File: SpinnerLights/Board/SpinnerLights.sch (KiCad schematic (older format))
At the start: 4 parts

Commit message: WIP on SpinnerLights board
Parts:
- removed C?: CP, symbol Device:CP
- removed R?: R, symbol Device:R
- added BT1: Battery_Cell, symbol Device:Battery_Cell
- added C1: 0.1uF, symbol Device:C
- added D1: D, symbol Device:D
- added JP1, JP?: Jumper_2_Open, symbol Jumper:Jumper_2_Open
- added PIXEL2, PIXEL3, PIXEL4, PIXEL5, PIXEL6, Pixel1: NeoPixel_THT, symbol LED:NeoPixel_THT
- added R1: 10K, symbol Device:R
- added R2: 5K, symbol Device:R
- added R3: 400, symbol Device:R
- added U2: ADXL343, Package_LGA:LGA-14_3x5mm_P0.8mm_LayoutBorder1x6y, symbol Sensor_Motion:ADXL343
- gave numbers to parts that had none: 2
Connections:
- net at BT2.1 (+): now also U1.15 (5V)
- net at BT2.2 (-): now also BT1.1 (+)
- net INT1: now reaches U1.10 (PA5_A9_D9_MISO)
- net INT1: now also U2.8 (INT1)
- net +3V3: now reaches U1.12 (3V3)
- net +3V3: now also C1.1, JP?.2 (B), PIXEL2.3 (VDD), PIXEL3.3 (VDD), Pixel1.3 (VDD), R1.2, U2.1 (Vdd_I/O), U2.6 (Vs)
- net GND: now reaches U1.13 (GND)
- net GND: now also U1.20 (GND), C1.2, PIXEL2.2 (GND), PIXEL3.2 (GND), PIXEL4.2 (GND), PIXEL5.2 (GND), PIXEL6.2 (GND), Pixel1.2 (GND), R2.2, U2.2 (GND), U2.4 (GND), U2.5 (GND)
- net at U1.16 (GND): now also BT1.2 (-)
- net at U1.2 (PA4_A1_D1): now also R3.2
- net SDA: now reaches U1.5 (PA8_A4_D4_SDA)
- net SDA: now also U2.13 (SDA/SDI/SDIO)
- net SCL: now reaches U1.6 (PA9_A5_D5_SCL)
- net SCL: now also U2.14 (SCL/SCLK)
- net INT2: now reaches U1.9 (PA7_A8_D8_SCK)
- net INT2: now also U2.9 (INT2)
- new net: D1.1 (K), JP1.1 (A)
- new net: D1.2 (A), R1.1, U2.12 (SDO/ADDR), U2.7 (~CS)
- new net: JP1.2 (B), R2.1
- new net: PIXEL2.4 (DIN), Pixel1.1 (DOUT)
- new net: Pixel1.4 (DIN), R3.1
- new net: PIXEL2.1 (DOUT), PIXEL3.4 (DIN)
- new net: PIXEL3.1 (DOUT), PIXEL6.4 (DIN)
- new net: PIXEL5.4 (DIN), PIXEL6.1 (DOUT)
- new net: JP?.1 (A), PIXEL4.3 (VDD), PIXEL5.3 (VDD), PIXEL6.3 (VDD)
- new net: PIXEL4.4 (DIN), PIXEL5.1 (DOUT)
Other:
- moved on the sheet: BT2, U1

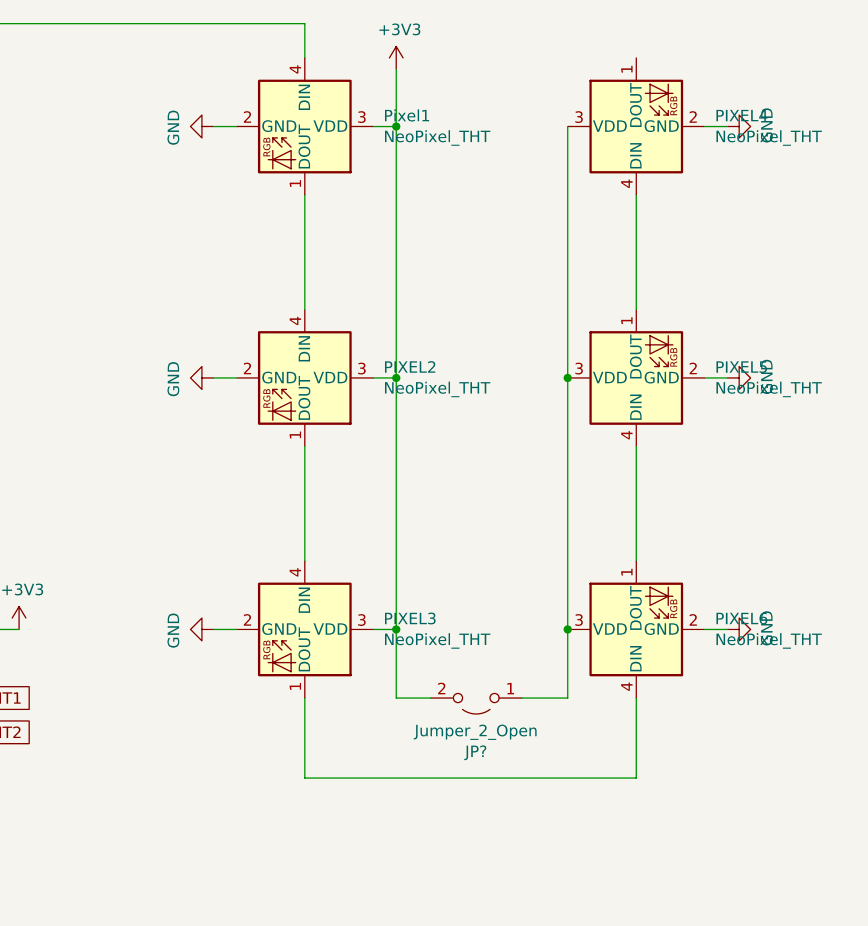
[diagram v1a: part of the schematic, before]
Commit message: SpinnerLights: Initial netlist and schematics
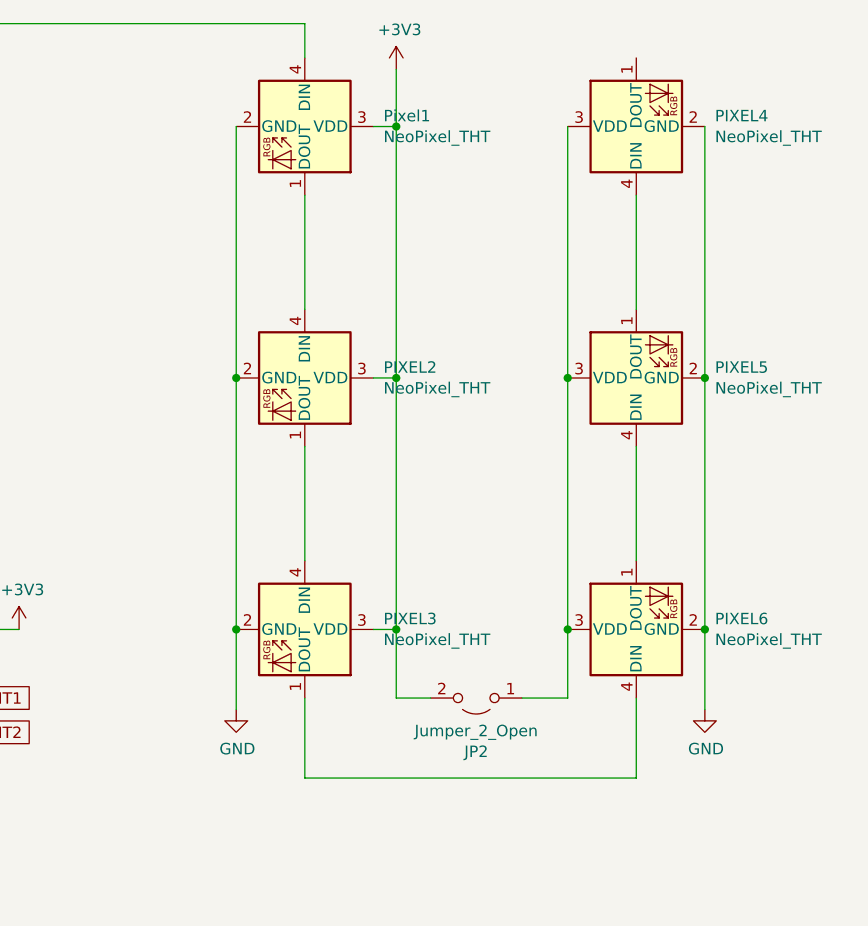
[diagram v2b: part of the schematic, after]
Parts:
- BT1, BT2: footprint (none) -> BAT-HLD-001-THM:BAT_BAT-HLD-001-THM
- C1: footprint (none) -> Capacitor_SMD:C_0805_2012Metric
- D1: footprint (none) -> Diode_SMD:D_0603_1608Metric_Pad1.05x0.95mm_HandSolder
- JP1: footprint (none) -> Jumper:SolderJumper-2_P1.3mm_Open_RoundedPad1.0x1.5mm
- JP2: renamed from JP?; footprint (none) -> Jumper:SolderJumper-2_P1.3mm_Open_RoundedPad1.0x1.5mm
- PIXEL2, PIXEL3, PIXEL4, PIXEL5, PIXEL6, Pixel1: footprint (none) -> LED_SMD:LED_SK6812MINI_PLCC4_3.5x3.5mm_P1.75mm
- R1, R2, R3: footprint (none) -> Resistor_SMD:R_0805_2012Metric_Pad1.20x1.40mm_HandSolder
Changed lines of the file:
@@
 F 0 "D1" H 1700 5167 50  0000 C CNN
 F 1 "D" H 1700 5076 50  0000 C CNN
-F 2 "" H 1700 4950 50  0001 C CNN
+F 2 "Diode_SMD:D_0603_1608Metric_Pad1.05x0.95mm_HandSolder" H 1700 4950 50  0001 C CNN
 F 3 "~" H 1700 4950 50  0001 C CNN
 	1    1700 4950
@@
 $EndComp
 $Comp
-L power:GND #PWR?
+L power:GND #PWR01
 U 1 1 616648C6
 P 1700 6700
-F 0 "#PWR?" H 1700 6450 50  0001 C CNN
+F 0 "#PWR01" H 1700 6450 50  0001 C CNN
 F 1 "GND" H 1705 6527 50  0000 C CNN
 F 2 "" H 1700 6700 50  0001 C CNN
@@
 F 0 "R1" H 2370 4896 50  0000 L CNN
 F 1 "10K" H 2370 4805 50  0000 L CNN
-F 2 "" V 2230 4850 50  0001 C CNN
+F 2 "Resistor_SMD:R_0805_2012Metric_Pad1.20x1.40mm_HandSolder" V 2230 4850 50  0001 C CNN
 F 3 "~" H 2300 4850 50  0001 C CNN
 	1    2300 4850
@@
 	2300 4550 2300 4700
 $Comp
-L power:+3V3 #PWR?
+L power:+3V3 #PWR02
 U 1 1 6166C856
 P 2300 5200
-F 0 "#PWR?" H 2300 5050 50  0001 C CNN
+F 0 "#PWR02" H 2300 5050 50  0001 C CNN
 F 1 "+3V3" H 2315 5373 50  0000 C CNN
 F 2 "" H 2300 5200 50  0001 C CNN
@@
 	2300 5000 2300 5200
 $Comp
-L power:GND #PWR?
+L power:GND #PWR05
 U 1 1 6166D36D
 P 6550 2750
-F 0 "#PWR?" H 6550 2500 50  0001 C CNN
+F 0 "#PWR05" H 6550 2500 50  0001 C CNN
 F 1 "GND" H 6555 2577 50  0000 C CNN
 F 2 "" H 6550 2750 50  0001 C CNN
@@
 F 0 "JP1" H 1700 5835 50  0000 C CNN
 F 1 "Jumper_2_Open" H 1700 5744 50  0000 C CNN
-F 2 "" H 1700 5600 50  0001 C CNN
+F 2 "Jumper:SolderJumper-2_P1.3mm_Open_RoundedPad1.0x1.5mm" H 1700 5600 50  0001 C CNN
 F 3 "~" H 1700 5600 50  0001 C CNN
 	1    1700 5600
@@
 F 0 "R2" H 1770 6296 50  0000 L CNN
 F 1 "5K" H 1770 6205 50  0000 L CNN
-F 2 "" V 1630 6250 50  0001 C CNN
+F 2 "Resistor_SMD:R_0805_2012Metric_Pad1.20x1.40mm_HandSolder" V 1630 6250 50  0001 C CNN
 F 3 "~" H 1700 6250 50  0001 C CNN
 	1    1700 6250
@@
 	1700 6400 1700 6700
 $Comp
-L power:+3V3 #PWR?
+L power:+3V3 #PWR07
 U 1 1 61671FEA
 P 7650 3800
-F 0 "#PWR?" H 7650 3650 50  0001 C CNN
+F 0 "#PWR07" H 7650 3650 50  0001 C CNN
 F 1 "+3V3" H 7665 3973 50  0000 C CNN
 F 2 "" H 7650 3800 50  0001 C CNN
@@
 	7100 3800 7650 3800
 $Comp
-L power:GND #PWR?
+L power:GND #PWR06
 U 1 1 61672DC1
 P 7450 3650
-F 0 "#PWR?" H 7450 3400 50  0001 C CNN
+F 0 "#PWR06" H 7450 3400 50  0001 C CNN
 F 1 "GND" H 7455 3477 50  0000 C CNN
 F 2 "" H 7450 3650 50  0001 C CNN
@@
 	2300 4250 2300 4550
 $Comp
-L power:GND #PWR?
+L power:GND #PWR03
 U 1 1 616882FF
 P 3200 5100
-F 0 "#PWR?" H 3200 4850 50  0001 C CNN
+F 0 "#PWR03" H 3200 4850 50  0001 C CNN
 F 1 "GND" H 3205 4927 50  0000 C CNN
 F 2 "" H 3200 5100 50  0001 C CNN
@@
 	3200 4850 3200 5000
 $Comp
-L power:+3V3 #PWR?
+L power:+3V3 #PWR04
 U 1 1 61689627
 P 3400 3650
-F 0 "#PWR?" H 3400 3500 50  0001 C CNN
+F 0 "#PWR04" H 3400 3500 50  0001 C CNN
 F 1 "+3V3" H 3415 3823 50  0000 C CNN
 F 2 "" H 3400 3650 50  0001 C CNN
@@
 F 0 "C1" H 4715 4046 50  0000 L CNN
 F 1 "0.1uF" H 4715 3955 50  0000 L CNN
-F 2 "" H 4638 3850 50  0001 C CNN
+F 2 "Capacitor_SMD:C_0805_2012Metric" H 4638 3850 50  0001 C CNN
 F 3 "~" H 4600 4000 50  0001 C CNN
 	1    4600 4000
@@
 F 0 "Pixel1" V 8854 1944 50  0000 L CNN
 F 1 "NeoPixel_THT" V 8945 1944 50  0000 L CNN
-F 2 "" H 8950 1300 50  0001 L TNN
+F 2 "LED_SMD:LED_SK6812MINI_PLCC4_3.5x3.5mm_P1.75mm" H 8950 1300 50  0001 L TNN
 F 3 "https://www.adafruit.com/product/1938" H 9000 1225 50  0001 L TNN
 	1    8900 1600
@@
 F 0 "R3" H 5170 3296 50  0000 L CNN
 F 1 "400" H 5170 3205 50  0000 L CNN
-F 2 "" V 5030 3250 50  0001 C CNN
+F 2 "Resistor_SMD:R_0805_2012Metric_Pad1.20x1.40mm_HandSolder" V 5030 3250 50  0001 C CNN
 F 3 "~" H 5100 3250 50  0001 C CNN
 	1    5100 3250
@@
 	5100 3650 5100 3400
 $Comp
-L power:+3V3 #PWR?
+L power:+3V3 #PWR011
 U 1 1 616A7416
 P 9300 1350
-F 0 "#PWR?" H 9300 1200 50  0001 C CNN
+F 0 "#PWR011" H 9300 1200 50  0001 C CNN
 F 1 "+3V3" H 9315 1523 50  0000 C CNN
 F 2 "" H 9300 1350 50  0001 C CNN
@@
 	1    0    0    -1
 $EndComp
-$Comp
-L power:GND #PWR?
-U 1 1 616A7F93
-P 8500 1600
-F 0 "#PWR?" H 8500 1350 50  0001 C CNN
-F 1 "GND" H 8505 1427 50  0000 C CNN
-F 2 "" H 8500 1600 50  0001 C CNN
-F 3 "" H 8500 1600 50  0001 C CNN
-	1    8500 1600
-	0    1    1    0
-$EndComp
 Wire Wire Line
 	9200 1600 9300 1600
-Wire Wire Line
-	8600 1600 8500 1600
 $Comp
 L LED:NeoPixel_THT PIXEL2
@@
 F 0 "PIXEL2" V 8854 3044 50  0000 L CNN
 F 1 "NeoPixel_THT" V 8945 3044 50  0000 L CNN
-F 2 "" H 8950 2400 50  0001 L TNN
+F 2 "LED_SMD:LED_SK6812MINI_PLCC4_3.5x3.5mm_P1.75mm" H 8950 2400 50  0001 L TNN
 F 3 "https://www.adafruit.com/product/1938" H 9000 2325 50  0001 L TNN
 	1    8900 2700
 	0    1    1    0
 $EndComp
-$Comp
-L power:GND #PWR?
-U 1 1 616B2926
-P 8500 2700
-F 0 "#PWR?" H 8500 2450 50  0001 C CNN
-F 1 "GND" H 8505 2527 50  0000 C CNN
-F 2 "" H 8500 2700 50  0001 C CNN
-F 3 "" H 8500 2700 50  0001 C CNN
-	1    8500 2700
-	0    1    1    0
-$EndComp
 Wire Wire Line
 	9200 2700 9300 2700
-Wire Wire Line
-	8600 2700 8500 2700
 $Comp
 L LED:NeoPixel_THT PIXEL3
@@
 F 0 "PIXEL3" V 8854 4144 50  0000 L CNN
 F 1 "NeoPixel_THT" V 8945 4144 50  0000 L CNN
-F 2 "" H 8950 3500 50  0001 L TNN
+F 2 "LED_SMD:LED_SK6812MINI_PLCC4_3.5x3.5mm_P1.75mm" H 8950 3500 50  0001 L TNN
 F 3 "https://www.adafruit.com/product/1938" H 9000 3425 50  0001 L TNN
 	1    8900 3800
 	0    1    1    0
 $EndComp
-$Comp
-L power:GND #PWR?
-U 1 1 616B4397
-P 8500 3800
-F 0 "#PWR?" H 8500 3550 50  0001 C CNN
-F 1 "GND" H 8505 3627 50  0000 C CNN
-F 2 "" H 8500 3800 50  0001 C CNN
-F 3 "" H 8500 3800 50  0001 C CNN
-	1    8500 3800
-	0    1    1    0
-$EndComp
 Wire Wire Line
 	9200 3800 9300 3800
-Wire Wire Line
-	8600 3800 8500 3800
 Wire Wire Line
 	5100 1150 8900 1150
@@
 F 0 "PIXEL6" V 10396 3456 50  0000 R CNN
 F 1 "NeoPixel_THT" V 10305 3456 50  0000 R CNN
-F 2 "" H 10400 3500 50  0001 L TNN
+F 2 "LED_SMD:LED_SK6812MINI_PLCC4_3.5x3.5mm_P1.75mm" H 10400 3500 50  0001 L TNN
 F 3 "https://www.adafruit.com/product/1938" H 10450 3425 50  0001 L TNN
 	1    10350 3800
 	0    -1   -1   0
 $EndComp
-$Comp
-L power:GND #PWR?
-U 1 1 616C9BA8
-P 10750 3800
-F 0 "#PWR?" H 10750 3550 50  0001 C CNN
-F 1 "GND" H 10755 3627 50  0000 C CNN
-F 2 "" H 10750 3800 50  0001 C CNN
-F 3 "" H 10750 3800 50  0001 C CNN
-	1    10750 3800
-	0    -1   -1   0
-$EndComp
-Wire Wire Line
-	10650 3800 10750 3800
 $Comp
 L LED:NeoPixel_THT PIXEL5
@@
 F 0 "PIXEL5" V 10396 2356 50  0000 R CNN
 F 1 "NeoPixel_THT" V 10305 2356 50  0000 R CNN
-F 2 "" H 10400 2400 50  0001 L TNN
+F 2 "LED_SMD:LED_SK6812MINI_PLCC4_3.5x3.5mm_P1.75mm" H 10400 2400 50  0001 L TNN
 F 3 "https://www.adafruit.com/product/1938" H 10450 2325 50  0001 L TNN
 	1    10350 2700
 	0    -1   -1   0
 $EndComp
-$Comp
-L power:GND #PWR?
-U 1 1 616C9BBC
-P 10750 2700
-F 0 "#PWR?" H 10750 2450 50  0001 C CNN
-F 1 "GND" H 10755 2527 50  0000 C CNN
-F 2 "" H 10750 2700 50  0001 C CNN
-F 3 "" H 10750 2700 50  0001 C CNN
-	1    10750 2700
-	0    -1   -1   0
-$EndComp
-Wire Wire Line
-	10650 2700 10750 2700
 $Comp
 L LED:NeoPixel_THT PIXEL4
@@
 F 0 "PIXEL4" V 10396 1256 50  0000 R CNN
 F 1 "NeoPixel_THT" V 10305 1256 50  0000 R CNN
-F 2 "" H 10400 1300 50  0001 L TNN
+F 2 "LED_SMD:LED_SK6812MINI_PLCC4_3.5x3.5mm_P1.75mm" H 10400 1300 50  0001 L TNN
 F 3 "https://www.adafruit.com/product/1938" H 10450 1225 50  0001 L TNN
 	1    10350 1600
 	0    -1   -1   0
 $EndComp
-$Comp
-L power:GND #PWR?
-U 1 1 616C9BD0
-P 10750 1600
-F 0 "#PWR?" H 10750 1350 50  0001 C CNN
-F 1 "GND" H 10755 1427 50  0000 C CNN
-F 2 "" H 10750 1600 50  0001 C CNN
-F 3 "" H 10750 1600 50  0001 C CNN
-	1    10750 1600
-	0    -1   -1   0
-$EndComp
-Wire Wire Line
-	10650 1600 10750 1600
 Wire Wire Line
 	10350 2400 10350 1900
@@
 	10350 3000 10350 3500
 $Comp
-L Jumper:Jumper_2_Open JP?
+L Jumper:Jumper_2_Open JP2
 U 1 1 616CB68A
 P 9650 4100
-F 0 "JP?" H 9650 4335 50  0000 C CNN
+F 0 "JP2" H 9650 4335 50  0000 C CNN
 F 1 "Jumper_2_Open" H 9650 4244 50  0000 C CNN
-F 2 "" H 9650 4100 50  0001 C CNN
+F 2 "Jumper:SolderJumper-2_P1.3mm_Open_RoundedPad1.0x1.5mm" H 9650 4100 50  0001 C CNN
 F 3 "~" H 9650 4100 50  0001 C CNN
 	1    9650 4100
@@
 F 0 "BT2" H 5818 5596 50  0000 L CNN
 F 1 "Battery_Cell" H 5818 5505 50  0000 L CNN
-F 2 "" V 5700 5560 50  0001 C CNN
+F 2 "BAT-HLD-001-THM:BAT_BAT-HLD-001-THM" V 5700 5560 50  0001 C CNN
 F 3 "~" V 5700 5560 50  0001 C CNN
 	1    5700 5500
@@
 F 0 "BT1" H 5818 6096 50  0000 L CNN
 F 1 "Battery_Cell" H 5818 6005 50  0000 L CNN
-F 2 "" V 5700 6060 50  0001 C CNN
+F 2 "BAT-HLD-001-THM:BAT_BAT-HLD-001-THM" V 5700 6060 50  0001 C CNN
 F 3 "~" V 5700 6060 50  0001 C CNN
 	1    5700 6000
@@
 Wire Wire Line
 	5700 6100 6400 6100
+$Comp
+L power:GND #PWR014
+U 1 1 616C9BA8
+P 10650 4150
+F 0 "#PWR014" H 10650 3900 50  0001 C CNN
+F 1 "GND" H 10655 3977 50  0000 C CNN
+F 2 "" H 10650 4150 50  0001 C CNN
+F 3 "" H 10650 4150 50  0001 C CNN
+	1    10650 4150
+	1    0    0    -1
+$EndComp
+Wire Wire Line
+	10650 1600 10650 2700
+Wire Wire Line
+	10650 2700 10650 3800
+Connection ~ 10650 2700
+Wire Wire Line
+	10650 3800 10650 4150
+Connection ~ 10650 3800
+$Comp
+L power:GND #PWR0101
+U 1 1 616F33F2
+P 8600 4150
+F 0 "#PWR0101" H 8600 3900 50  0001 C CNN
+F 1 "GND" H 8605 3977 50  0000 C CNN
+F 2 "" H 8600 4150 50  0001 C CNN
+F 3 "" H 8600 4150 50  0001 C CNN
+	1    8600 4150
+	1    0    0    -1
+$EndComp
+Wire Wire Line
+	8600 4150 8600 3800
+Wire Wire Line
+	8600 3800 8600 2700
+Connection ~ 8600 3800
+Wire Wire Line
+	8600 2700 8600 1600
+Connection ~ 8600 2700
 Wire Wire Line
 	6200 4800 5700 4800

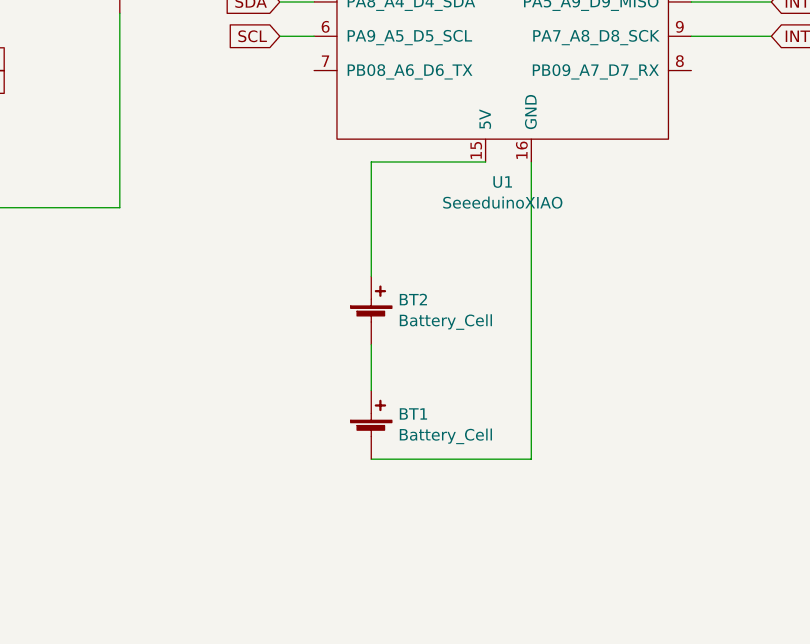
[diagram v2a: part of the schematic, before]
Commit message: SpinnerLights: Initial board generation
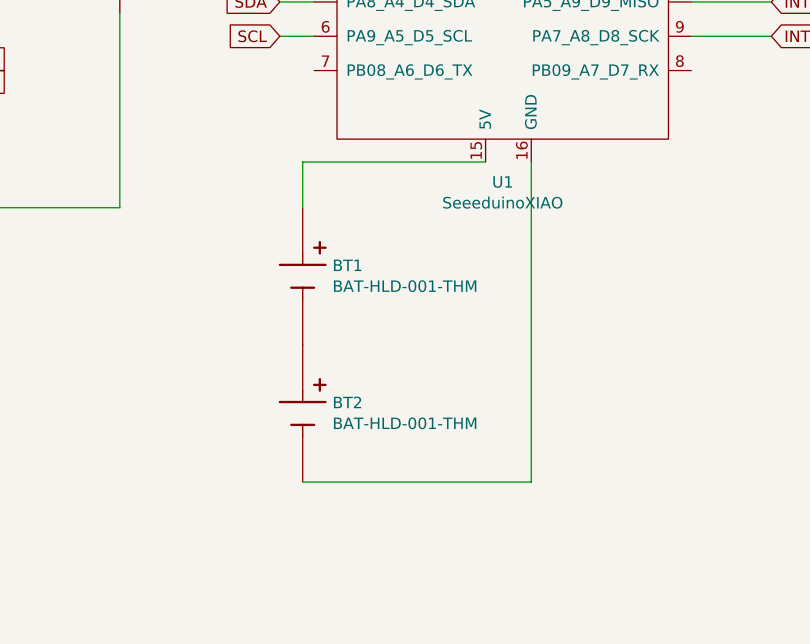
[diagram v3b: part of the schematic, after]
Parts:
- removed BT1, BT2: Battery_Cell, BAT-HLD-001-THM:BAT_BAT-HLD-001-THM, symbol Device:Battery_Cell
- added BT1, BT2: BAT-HLD-001-THM, BAT_BAT-HLD-001-THM, symbol BAT-HLD-001-THM:BAT-HLD-001-THM
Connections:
- net at U1.15 (5V): now also BT1.P1, BT1.P2, BT1.P3, BT1.P4
- net at U1.16 (GND): now also BT2.N
- new net: BT1.N, BT2.P1, BT2.P2, BT2.P3, BT2.P4
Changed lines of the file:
@@
 Wire Wire Line
 	8900 1150 8900 1300
-Wire Wire Line
-	6400 4800 6400 6100
-$Comp
-L Device:Battery_Cell BT2
-U 1 1 6165CE41
-P 5700 5500
-F 0 "BT2" H 5818 5596 50  0000 L CNN
-F 1 "Battery_Cell" H 5818 5505 50  0000 L CNN
-F 2 "BAT-HLD-001-THM:BAT_BAT-HLD-001-THM" V 5700 5560 50  0001 C CNN
-F 3 "~" V 5700 5560 50  0001 C CNN
-	1    5700 5500
-	1    0    0    -1
-$EndComp
-$Comp
-L Device:Battery_Cell BT1
-U 1 1 616660DA
-P 5700 6000
-F 0 "BT1" H 5818 6096 50  0000 L CNN
-F 1 "Battery_Cell" H 5818 6005 50  0000 L CNN
-F 2 "BAT-HLD-001-THM:BAT_BAT-HLD-001-THM" V 5700 6060 50  0001 C CNN
-F 3 "~" V 5700 6060 50  0001 C CNN
-	1    5700 6000
-	1    0    0    -1
-$EndComp
-Wire Wire Line
-	5700 5800 5700 5600
-Wire Wire Line
-	5700 6100 6400 6100
 $Comp
 L power:GND #PWR014
@@
 	8600 2700 8600 1600
 Connection ~ 8600 2700
+$Comp
+L BAT-HLD-001-THM:BAT-HLD-001-THM BT2
+U 1 1 617077E9
+P 5400 5900
+F 0 "BT2" V 5354 6030 50  0000 L CNN
+F 1 "BAT-HLD-001-THM" V 5445 6030 50  0000 L CNN
+F 2 "BAT_BAT-HLD-001-THM" H 5400 5900 50  0001 L BNN
+F 3 "" H 5400 5900 50  0001 L BNN
+F 4 "Manufacturer Recommendations" H 5400 5900 50  0001 L BNN "STANDARD"
+F 5 "C" H 5400 5900 50  0001 L BNN "PARTREV"
+F 6 "Linx Technologies" H 5400 5900 50  0001 L BNN "MANUFACTURER"
+F 7 "4.2mm" H 5400 5900 50  0001 L BNN "MAXIMUM_PACKAGE_HEIGHT"
+	1    5400 5900
+	0    1    1    0
+$EndComp
+$Comp
+L BAT-HLD-001-THM:BAT-HLD-001-THM BT1
+U 1 1 61708CB4
+P 5400 5300
+F 0 "BT1" V 5354 5430 50  0000 L CNN
+F 1 "BAT-HLD-001-THM" V 5445 5430 50  0000 L CNN
+F 2 "BAT_BAT-HLD-001-THM" H 5400 5300 50  0001 L BNN
+F 3 "" H 5400 5300 50  0001 L BNN
+F 4 "Manufacturer Recommendations" H 5400 5300 50  0001 L BNN "STANDARD"
+F 5 "C" H 5400 5300 50  0001 L BNN "PARTREV"
+F 6 "Linx Technologies" H 5400 5300 50  0001 L BNN "MANUFACTURER"
+F 7 "4.2mm" H 5400 5300 50  0001 L BNN "MAXIMUM_PACKAGE_HEIGHT"
+	1    5400 5300
+	0    1    1    0
+$EndComp
 Wire Wire Line
-	6200 4800 5700 4800
+	6400 6200 6400 4800
 Wire Wire Line
-	5700 4800 5700 5300
+	5400 6200 6400 6200
+Wire Wire Line
+	5400 4800 5400 5000
+Wire Wire Line
+	5400 4800 6200 4800
 $EndSCHEMATC
